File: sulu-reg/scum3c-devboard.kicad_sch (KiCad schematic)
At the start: 36 parts, among them J1 Conn_02x11_Odd_Even, J2 Conn_02x10_Odd_Even, J3 Conn_01x10, J4 73391-0060, U2 S-85S1AB18-I6T1U, U3 S-85S1AB11-I6T1U, U9AB1 ICM-20948

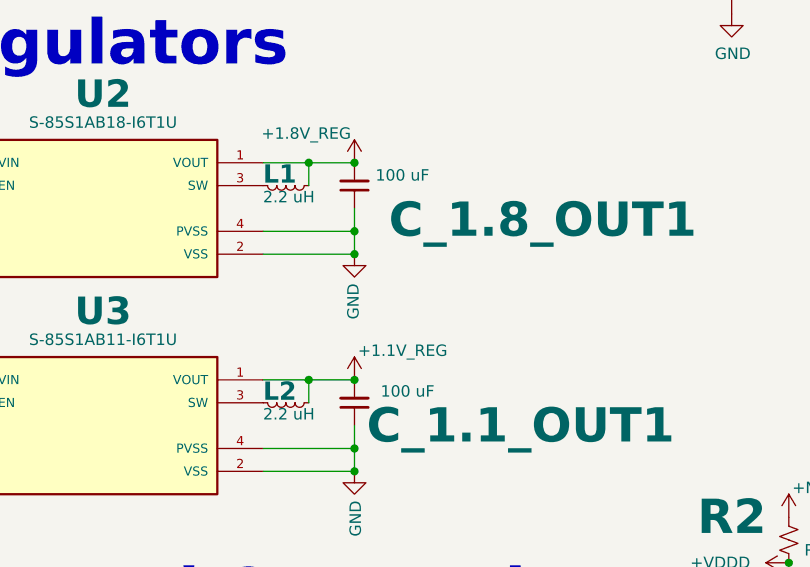
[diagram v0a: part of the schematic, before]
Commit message: Add ground stitching vias
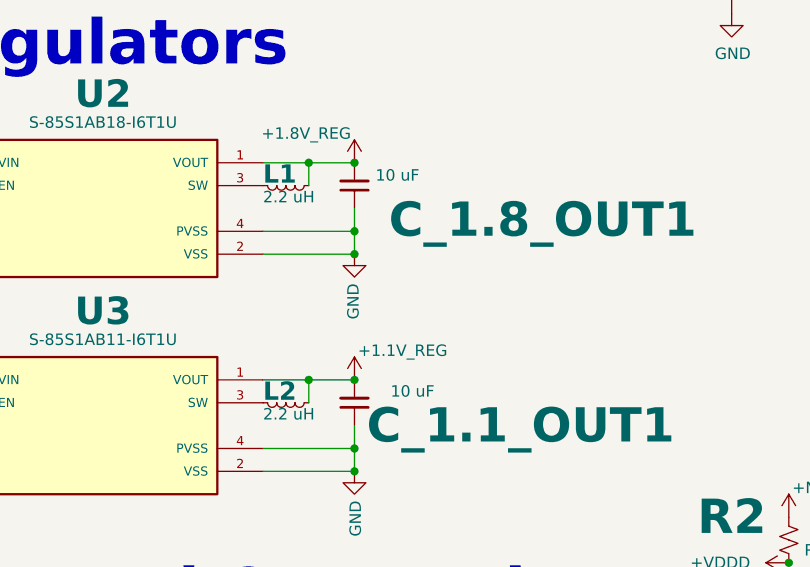
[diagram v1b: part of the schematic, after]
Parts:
- C_1.1_OUT1, C_1.8_OUT1: value 100 uF -> 10 uF
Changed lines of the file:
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@@
 			)
 		)
-		(property "Value" "100 uF"
+		(property "Value" "10 uF"
 			(at 78.5368 111.887 0)
 			(effects
@@
 			)
 		)
-		(property "Value" "100 uF"
+		(property "Value" "10 uF"
 			(at 85.09 135.89 0)
 			(effects
